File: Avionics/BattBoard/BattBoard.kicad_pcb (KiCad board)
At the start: 2 copper layers, 28 parts, among them J1 Screw_Terminal_01x01, J2 JST_PH_S2B-PH-SM4, Q1 IRF7458, Q2 IRF7458

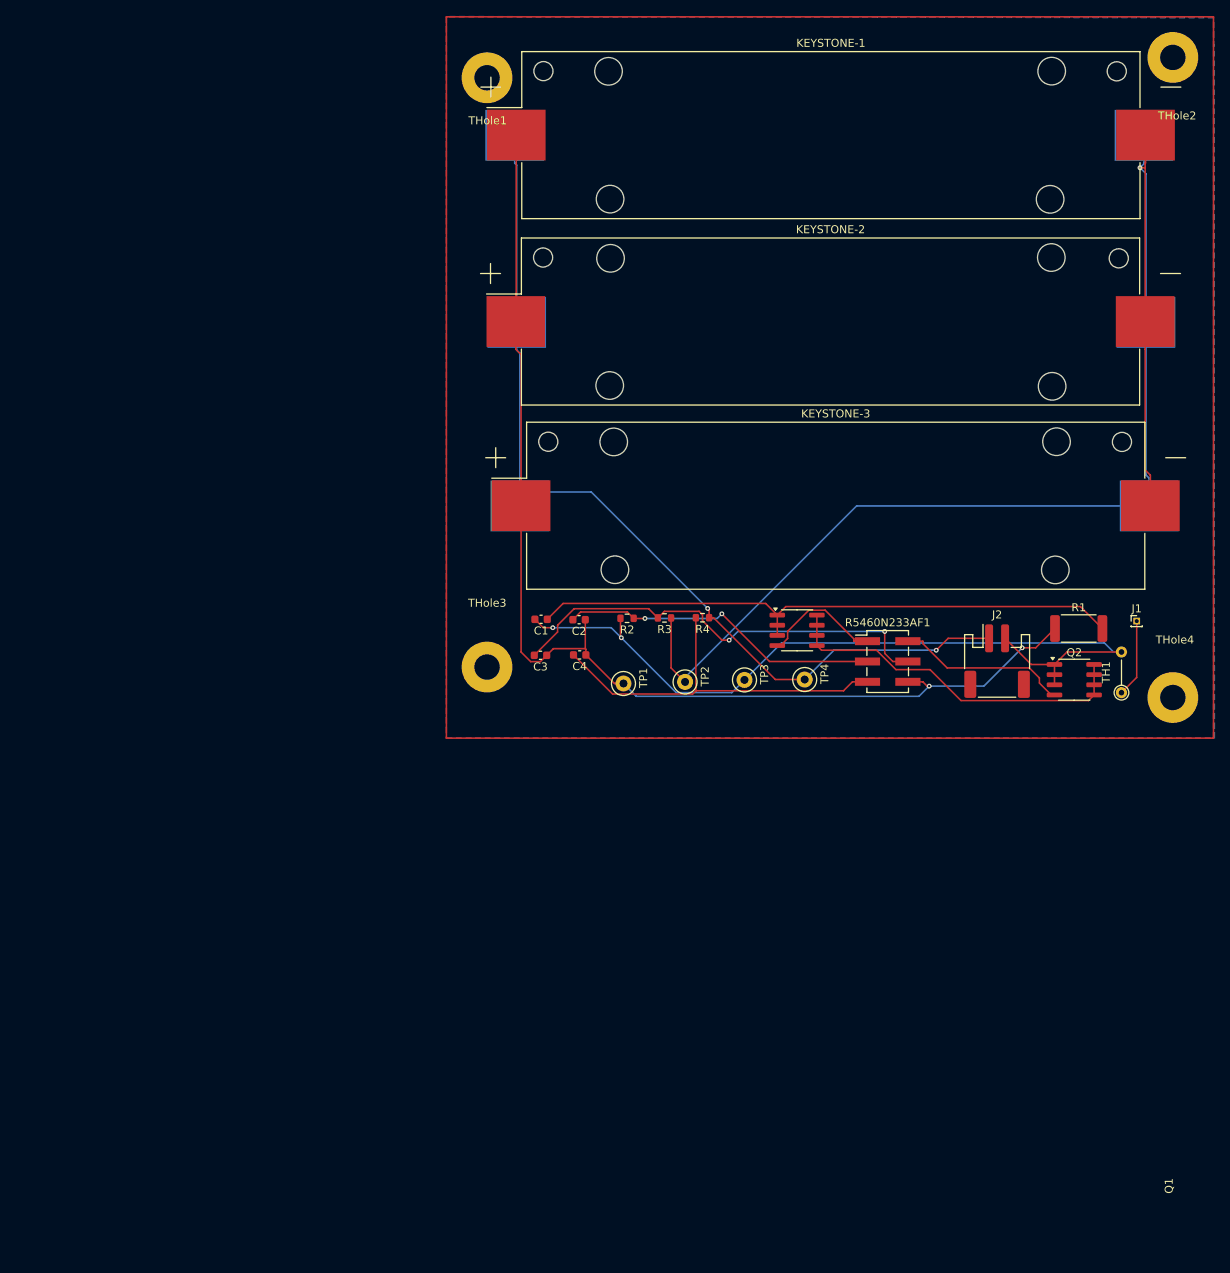
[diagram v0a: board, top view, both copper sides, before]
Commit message: Sephora Poteau: Cut the edges of the board and aligned it to PC104 layout
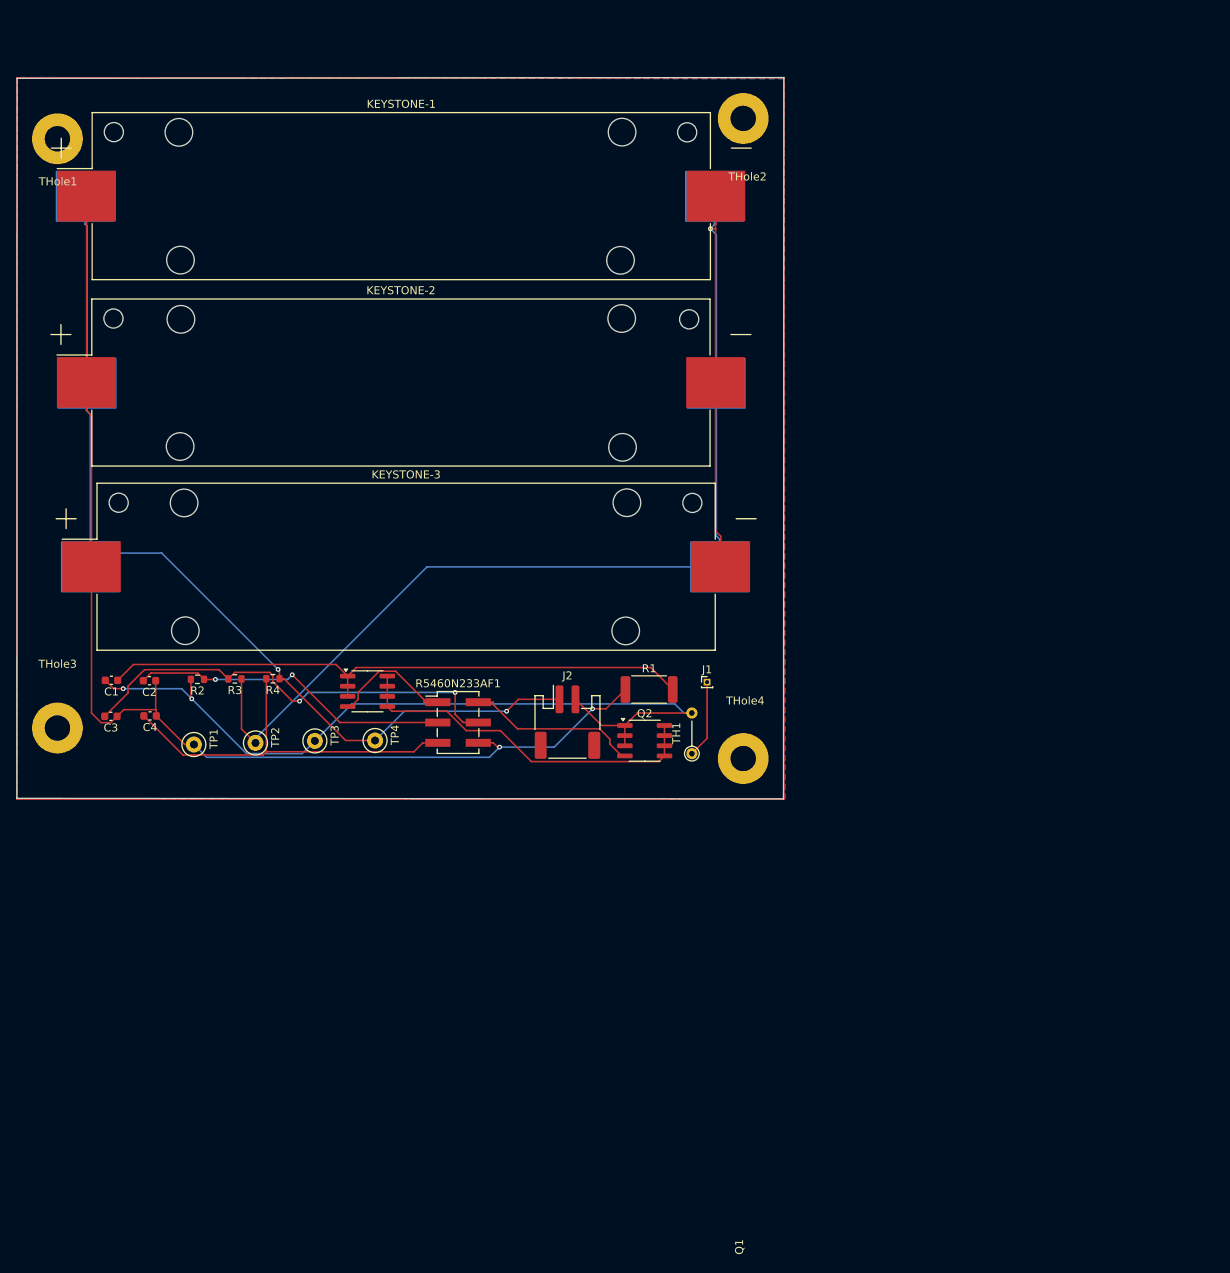
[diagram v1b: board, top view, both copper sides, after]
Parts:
- moved C3 54.2 mm to (104.5, 125.5)
- moved R3 54.2 mm to (120.0, 120.8)
- moved R4 54.2 mm to (124.7, 120.8)
- moved TP1 54.2 mm to (114.8, 129.1)
- moved C1 54.2 mm to (104.5, 121.0)
- moved C2 54.2 mm to (109.3, 121.1)
- moved J1 54.2 mm to (179.0, 121.2)
- moved J2 54.2 mm to (161.5, 126.2)
- moved KEYSTONE-1 54.2 mm to (140.8, 60.5)
- moved KEYSTONE-2 54.2 mm to (140.7, 83.8)
- moved KEYSTONE-3 54.2 mm to (141.4, 106.8)
- moved KEYSTONE-4 54.2 mm to (140.6, 60.5)
- moved KEYSTONE-5 54.2 mm to (140.8, 83.9)
- moved KEYSTONE-6 54.2 mm to (141.2, 106.8)
- moved Q1 54.2 mm to (136.5, 122.4)
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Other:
- board outline added: 95.9 x 90.2 mm

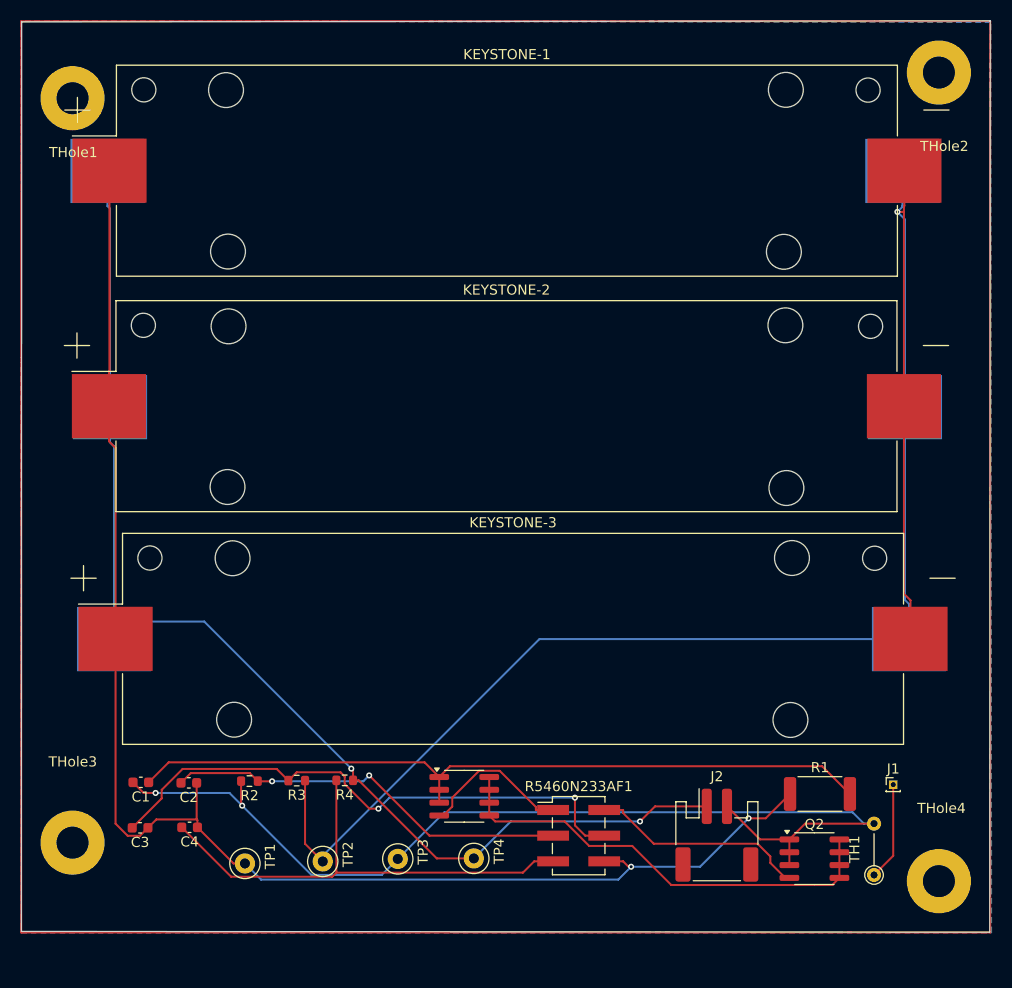
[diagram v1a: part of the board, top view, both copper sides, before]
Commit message: Sephora Poteau: Added temperature sensor and terminal block connectors to Battery Board
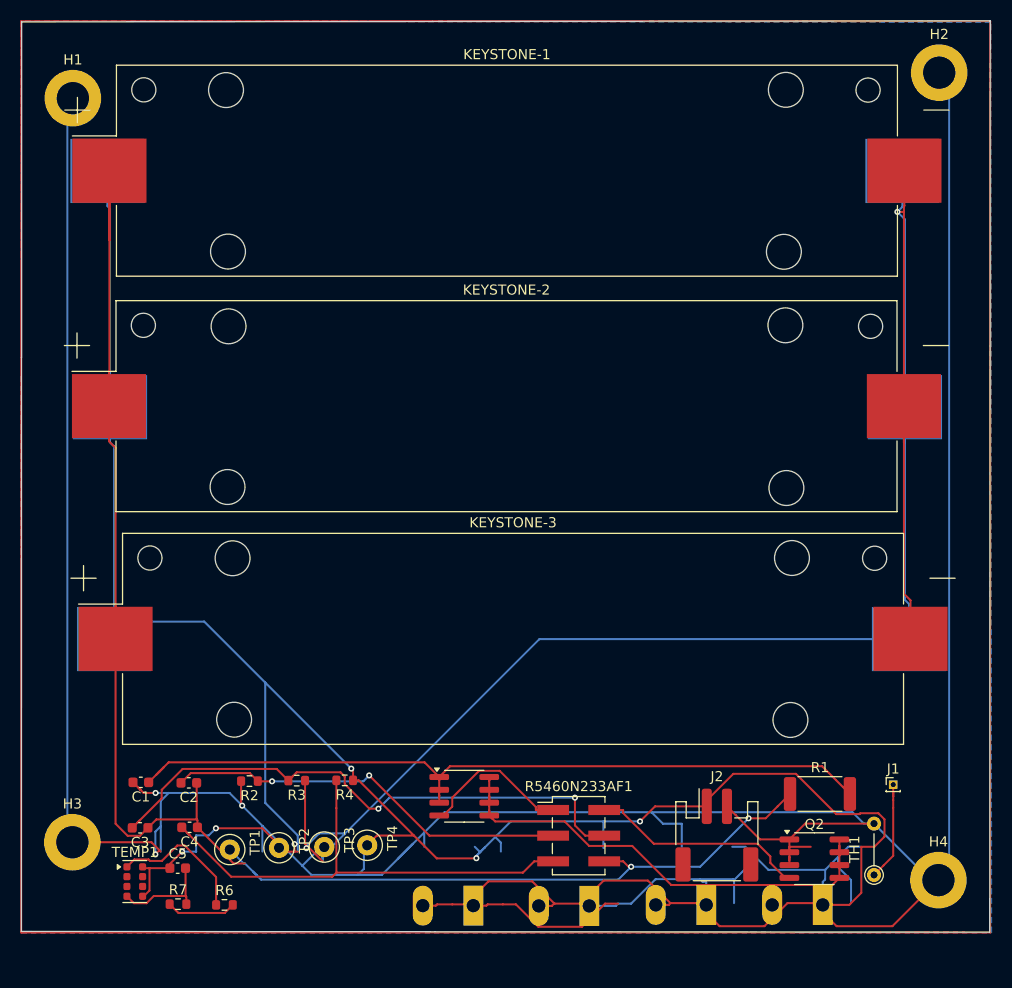
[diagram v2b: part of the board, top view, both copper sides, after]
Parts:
- removed THole1, THole2, THole3, THole4: PC104TH, GlobalLib:PC104TH
- added C5: C, Capacitor_SMD:C_0603_1608Metric, F.Cu at (108.2, 129.5)
- added H1: MountingHole_Pad, MountingHole:MountingHole_3.2mm_M3_DIN965_Pad, F.Cu at (97.8, 53.3)
- added H2: MountingHole_Pad, MountingHole:MountingHole_3.2mm_M3_DIN965_Pad, F.Cu at (183.6, 50.8)
- added H3: MountingHole_Pad, MountingHole:MountingHole_3.2mm_M3_DIN965_Pad, F.Cu at (97.8, 127.0)
- added H4: MountingHole_Pad, MountingHole:MountingHole_3.2mm_M3_DIN965_Pad, F.Cu at (183.5, 130.7)
- added J3: Screw_Terminal_01x02, TerminalBlock:TerminalBlock_Altech_AK300-2_P5.00mm, B.Cu at (172.0, 133.2)
- added J4: Screw_Terminal_01x02, TerminalBlock:TerminalBlock_Altech_AK300-2_P5.00mm, B.Cu at (160.5, 133.2)
- added J5: Screw_Terminal_01x02, TerminalBlock:TerminalBlock_Altech_AK300-2_P5.00mm, B.Cu at (148.9, 133.2)
- added J6: Screw_Terminal_01x02, TerminalBlock:TerminalBlock_Altech_AK300-2_P5.00mm, B.Cu at (137.4, 133.2)
- added R6: R_US, Resistor_SMD:R_0603_1608Metric, F.Cu at (112.8, 133.2)
- added R7: R_US, Resistor_SMD:R_0603_1608Metric, F.Cu at (108.2, 133.1)
- added TEMP1: ~, Sensor:Rohm_RPR-0521RS, F.Cu at (104.0, 130.8)
- moved TP4 10.6 mm to (127.0, 127.2)
- moved TP3 7.37 mm to (122.7, 127.4)
- moved TP2 4.53 mm to (118.2, 127.5)
- moved TP1 2.03 mm to (113.3, 127.7)
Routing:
- net PACK-: track 101.7 -> 368.0 mm, vias 2 -> 3
- net PACK+: track 117.7 -> 270.3 mm, vias 2 -> 6
- net BM: track 170.4 -> 186.0 mm, vias 1 -> 2
- net Net-(TEMP1-VOUT): track 0.00 -> 13.9 mm
- net B-: track 145.7 -> 159.4 mm
- net GND: track 0.00 -> 9.97 mm
- net TEMP_PDU: track 0.00 -> 6.94 mm
- net Net-(Q1-D-Pad5): track 45.4 -> 49.0 mm
- net Net-(C1-Pad1): track 74.9 -> 77.2 mm

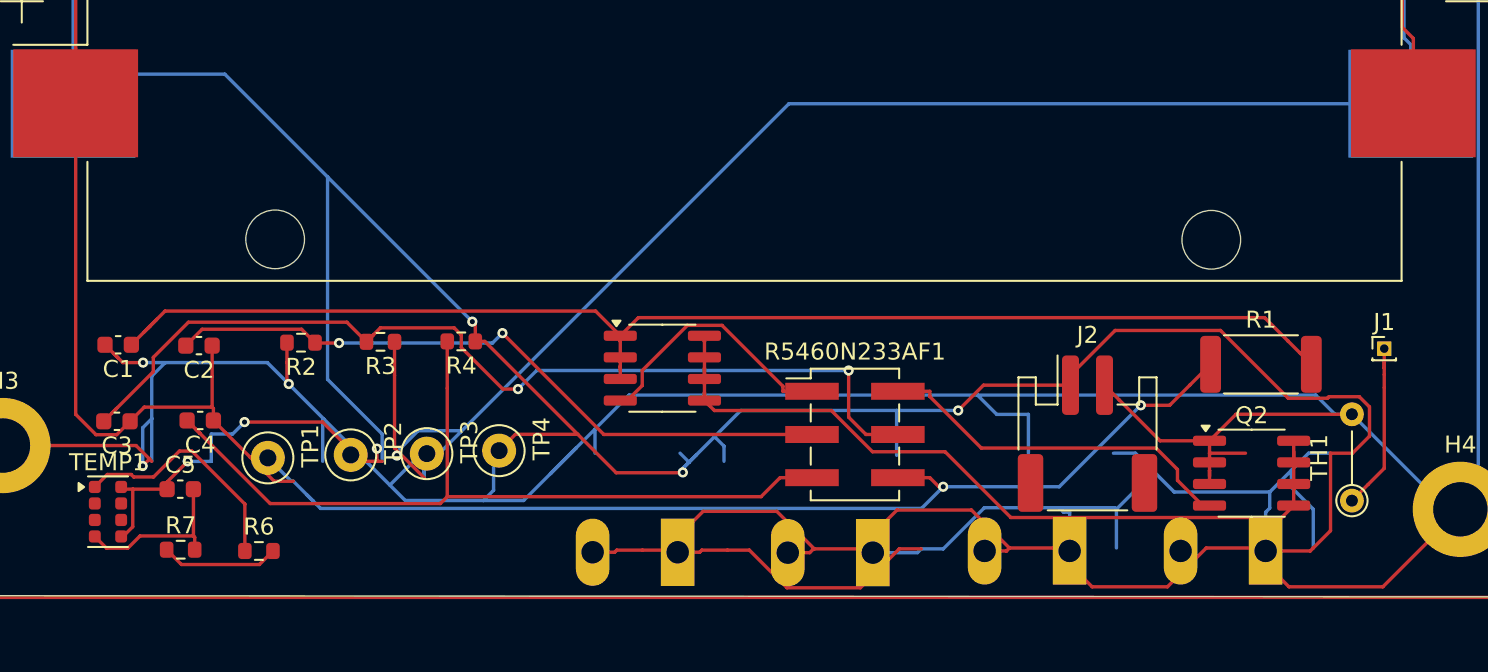
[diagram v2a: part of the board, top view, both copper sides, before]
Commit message: Ian Goldberg - Corrected DRC errors on battery board and generated gerber files to order
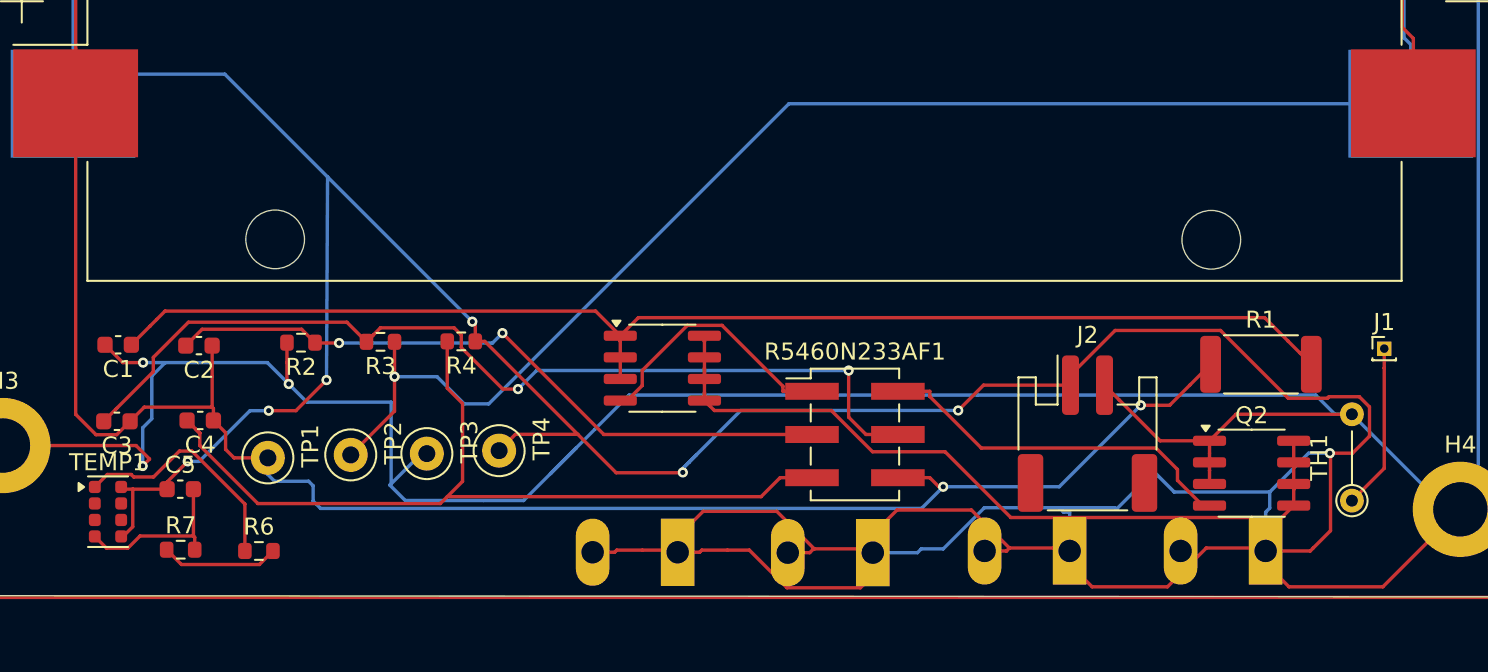
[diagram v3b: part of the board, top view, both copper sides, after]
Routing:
- net PACK+: track 270.3 -> 240.7 mm, vias 6 -> 7
- net PACK-: track 368.0 -> 353.2 mm
- net BM: track 186.0 -> 180.7 mm
- net B-: track 159.4 -> 157.5 mm
- net Net-(C1-Pad1): track 77.2 -> 75.5 mm
- net /VDD: track 48.9 -> 50.1 mm
